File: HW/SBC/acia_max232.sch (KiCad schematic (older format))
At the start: 11 parts, among them J1 Serial Port, U4 MAX232, U5 6551

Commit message: New MB design. Includes RTC. New IDE design.
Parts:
- removed Pad1: RI, Wire_Pads:SolderWirePad_single_0-8mmDrill, symbol Mounting_Hole_PAD
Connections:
- wire segments 59 -> 57
- no-connect marks 6 -> 7
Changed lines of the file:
@@
-$EndComp
-$Comp
-L Mounting_Hole_PAD Pad1
-U 1 1 58D7281F
-P 1475 3200
-F 0 "Pad1" H 1475 3450 50  0000 C CNN
-F 1 "RI" H 1475 3375 50  0000 C CNN
-F 2 "Wire_Pads:SolderWirePad_single_0-8mmDrill" H 1475 3200 50  0001 C CNN
-F 3 "" H 1475 3200 50  0001 C CNN
-	1    1475 3200
-	-1   0    0    1
 $EndComp
 $Comp
@@
 Wire Wire Line
 	3700 3550 3575 3550
-Wire Wire Line
-	1825 2850 1475 2850
-Wire Wire Line
-	1475 2850 1475 3100
 Wire Wire Line
 	4500 4350 4500 4625
@@
 Wire Wire Line
 	7975 4675 7975 4800
+NoConn ~ 1825 2850
 $EndSCHEMATC

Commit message: Updates to pcb and monitor.
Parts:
- added C17: 22pF, Capacitors_ThroughHole:C_Disc_D3.8mm_W2.6mm_P2.50mm, symbol C_Small
- J1: footprint Pin_Headers:Pin_Header_Straight_2x05_Pitch2.54mm -> Connect:IDC_Header_Straight_10pins
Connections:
- net GND: now also C6.1, C17.1; no longer C6.2
- net at U5.6 (XTLI), XTAL1.1: now also C17.2; no longer C6.1
- net at U5.7 (XTLO), XTAL1.2: now also C6.2
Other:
- moved on the sheet: C6
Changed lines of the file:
@@
 L C_Small C6
 U 1 1 58D702B2
-P 6450 2050
-F 0 "C6" H 6550 2100 50  0000 L CNN
-F 1 "22pF" H 6200 2125 50  0000 L CNN
-F 2 "Capacitors_ThroughHole:C_Disc_D3.8mm_W2.6mm_P2.50mm" H 6450 2050 50  0001 C CNN
-F 3 "" H 6450 2050 50  0001 C CNN
-	1    6450 2050
+P 6450 1600
+F 0 "C6" H 6550 1650 50  0000 L CNN
+F 1 "22pF" H 6200 1675 50  0000 L CNN
+F 2 "Capacitors_ThroughHole:C_Disc_D3.8mm_W2.6mm_P2.50mm" H 6450 1600 50  0001 C CNN
+F 3 "" H 6450 1600 50  0001 C CNN
+	1    6450 1600
 	1    0    0    -1
 $EndComp
@@
 L GND #PWR02
 U 1 1 58D7044A
-P 6450 2150
-F 0 "#PWR02" H 6450 1900 50  0001 C CNN
-F 1 "GND" H 6450 2000 50  0000 C CNN
-F 2 "" H 6450 2150 50  0001 C CNN
-F 3 "" H 6450 2150 50  0001 C CNN
-	1    6450 2150
-	1    0    0    -1
+P 6450 1500
+F 0 "#PWR02" H 6450 1250 50  0001 C CNN
+F 1 "GND" H 6450 1350 50  0000 C CNN
+F 2 "" H 6450 1500 50  0001 C CNN
+F 3 "" H 6450 1500 50  0001 C CNN
+	1    6450 1500
+	-1   0    0    1
 $EndComp
 Text GLabel 9150 3925 2    60   Input ~ 0
@@
 F 0 "J1" H 2075 2950 50  0000 C CNN
 F 1 "Serial Port" H 2075 2350 50  0000 C CNN
-F 2 "Pin_Headers:Pin_Header_Straight_2x05_Pitch2.54mm" H 2075 1450 50  0001 C CNN
+F 2 "Connect:IDC_Header_Straight_10pins" H 2075 1450 50  0001 C CNN
 F 3 "" H 2075 1450 50  0001 C CNN
 	1    2075 2650
@@
 	8675 3725 9150 3725
 Wire Wire Line
-	6450 1950 7275 1950
-Connection ~ 6925 1950
+	7275 1700 7275 1950
 Wire Wire Line
 	7275 2075 7150 2075
@@
 	7975 4675 7975 4800
 NoConn ~ 1825 2850
+$Comp
+L C_Small C17
+U 1 1 59018F37
+P 7275 1600
+F 0 "C17" H 7375 1650 50  0000 L CNN
+F 1 "22pF" H 7025 1675 50  0000 L CNN
+F 2 "Capacitors_ThroughHole:C_Disc_D3.8mm_W2.6mm_P2.50mm" H 7275 1600 50  0001 C CNN
+F 3 "" H 7275 1600 50  0001 C CNN
+	1    7275 1600
+	1    0    0    -1
+$EndComp
+$Comp
+L GND #PWR012
+U 1 1 59019537
+P 7275 1500
+F 0 "#PWR012" H 7275 1250 50  0001 C CNN
+F 1 "GND" H 7275 1350 50  0000 C CNN
+F 2 "" H 7275 1500 50  0001 C CNN
+F 3 "" H 7275 1500 50  0001 C CNN
+	1    7275 1500
+	-1   0    0    1
+$EndComp
+Wire Wire Line
+	6925 2150 6450 2150
+Wire Wire Line
+	7275 1950 6925 1950
+Wire Wire Line
+	6450 2150 6450 1700
 $EndSCHEMATC

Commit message: Move dicoupling capacitators as close the chips as possible.
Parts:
- added C?: 0.1uF, symbol C
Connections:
- net GND: now also C?.2
- net VCC: now also C?.1
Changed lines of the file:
@@
 	-1   0    0    1
 $EndComp
-Wire Wire Line
-	8675 1950 9150 1950
-Wire Wire Line
-	8675 2075 9150 2075
-Wire Wire Line
-	8675 2200 9150 2200
-Wire Wire Line
-	8675 2325 9150 2325
-Wire Wire Line
-	8675 2450 9150 2450
-Wire Wire Line
-	8675 2575 9150 2575
-Wire Wire Line
-	8675 2700 9150 2700
-Wire Wire Line
-	8675 2825 9150 2825
-Wire Wire Line
-	8675 3100 9150 3100
-Wire Wire Line
-	8675 3225 9150 3225
-Wire Wire Line
-	8675 3475 9500 3475
-Wire Wire Line
-	8675 3600 9150 3600
-Wire Wire Line
-	8675 3725 9150 3725
-Wire Wire Line
-	7275 1700 7275 1950
-Wire Wire Line
-	7275 2075 7150 2075
-Wire Wire Line
-	7150 2075 6925 2150
-Wire Wire Line
-	8675 4050 9150 4050
-Wire Wire Line
-	8675 4175 9150 4175
-Wire Wire Line
-	8675 3925 9150 3925
-Wire Wire Line
-	5300 4050 5425 4050
-Wire Wire Line
-	5425 3850 5300 3750
-Wire Wire Line
-	3700 4050 3575 4050
-Wire Wire Line
-	3575 3850 3700 3750
-Wire Wire Line
-	3700 3250 3575 3250
-Wire Wire Line
-	3375 3250 3050 3250
-Wire Wire Line
-	1825 2650 1650 2650
-Wire Wire Line
-	1650 2650 1650 3150
-Wire Wire Line
-	3700 3550 3575 3550
-Wire Wire Line
-	4500 4350 4500 4625
-Wire Wire Line
-	3050 4500 4925 4500
-Connection ~ 4500 4500
-Wire Wire Line
-	3375 3550 3050 3550
-Wire Wire Line
-	3050 3550 3050 4500
-Wire Wire Line
-	2325 2450 3700 2450
-Wire Wire Line
-	1825 2550 1725 2550
-Wire Wire Line
-	1725 2550 1725 2275
-Wire Wire Line
-	1725 2275 3475 2275
-Wire Wire Line
-	3475 2275 3475 2850
-Wire Wire Line
-	3475 2850 3700 2850
-Wire Wire Line
-	1825 2750 1750 2750
-Wire Wire Line
-	1750 2750 1750 3050
-Wire Wire Line
-	1750 3050 3700 3050
-Wire Wire Line
-	2325 2750 2925 2750
-Wire Wire Line
-	2925 2750 2925 2650
-Wire Wire Line
-	2925 2650 3700 2650
 NoConn ~ 2325 2550
 NoConn ~ 2325 2650
 NoConn ~ 2325 2850
 NoConn ~ 1825 2450
-Wire Wire Line
-	5300 2450 7275 2450
-Wire Wire Line
-	6650 2300 7275 2300
-Wire Wire Line
-	5300 3050 6850 3050
-Wire Wire Line
-	6850 3050 6850 2700
-Wire Wire Line
-	6850 2700 7275 2700
-Wire Wire Line
-	5300 2650 6300 2650
-Wire Wire Line
-	6300 2650 6300 2900
-Wire Wire Line
-	6300 2900 7275 2900
-Wire Wire Line
-	5300 2850 5925 2850
-Wire Wire Line
-	5925 2850 5925 2550
-Wire Wire Line
-	5925 2550 6650 2550
-Wire Wire Line
-	6650 2550 6650 2300
 $Comp
 L GND #PWR08
@@
 	1    0    0    -1
 $EndComp
-Wire Wire Line
-	7975 4675 7975 4800
 NoConn ~ 1825 2850
 $Comp
@@
 	-1   0    0    1
 $EndComp
+$Comp
+L C C?
+U 1 1 5905372B
+P 8125 4675
+F 0 "C?" V 8275 4625 50  0000 L CNN
+F 1 "0.1uF" V 7975 4650 50  0000 L CNN
+F 2 "" H 8163 4525 50  0001 C CNN
+F 3 "" H 8125 4675 50  0001 C CNN
+	1    8125 4675
+	0    1    1    0
+$EndComp
+Wire Wire Line
+	8675 1950 9150 1950
+Wire Wire Line
+	8675 2075 9150 2075
+Wire Wire Line
+	8675 2200 9150 2200
+Wire Wire Line
+	8675 2325 9150 2325
+Wire Wire Line
+	8675 2450 9150 2450
+Wire Wire Line
+	8675 2575 9150 2575
+Wire Wire Line
+	8675 2700 9150 2700
+Wire Wire Line
+	8675 2825 9150 2825
+Wire Wire Line
+	8675 3100 9150 3100
+Wire Wire Line
+	8675 3225 9150 3225
+Wire Wire Line
+	8675 3475 9500 3475
+Wire Wire Line
+	8675 3600 9150 3600
+Wire Wire Line
+	8675 3725 9150 3725
+Wire Wire Line
+	7275 1700 7275 1950
+Wire Wire Line
+	7275 2075 7150 2075
+Wire Wire Line
+	7150 2075 6925 2150
+Wire Wire Line
+	8675 4050 9150 4050
+Wire Wire Line
+	8675 4175 9150 4175
+Wire Wire Line
+	8675 3925 9150 3925
+Wire Wire Line
+	5300 4050 5425 4050
+Wire Wire Line
+	5425 3850 5300 3750
+Wire Wire Line
+	3700 4050 3575 4050
+Wire Wire Line
+	3575 3850 3700 3750
+Wire Wire Line
+	3700 3250 3575 3250
+Wire Wire Line
+	3375 3250 3050 3250
+Wire Wire Line
+	1825 2650 1650 2650
+Wire Wire Line
+	1650 2650 1650 3150
+Wire Wire Line
+	3700 3550 3575 3550
+Wire Wire Line
+	4500 4350 4500 4625
+Wire Wire Line
+	3050 4500 4925 4500
+Connection ~ 4500 4500
+Wire Wire Line
+	3375 3550 3050 3550
+Wire Wire Line
+	3050 3550 3050 4500
+Wire Wire Line
+	2325 2450 3700 2450
+Wire Wire Line
+	1825 2550 1725 2550
+Wire Wire Line
+	1725 2550 1725 2275
+Wire Wire Line
+	1725 2275 3475 2275
+Wire Wire Line
+	3475 2275 3475 2850
+Wire Wire Line
+	3475 2850 3700 2850
+Wire Wire Line
+	1825 2750 1750 2750
+Wire Wire Line
+	1750 2750 1750 3050
+Wire Wire Line
+	1750 3050 3700 3050
+Wire Wire Line
+	2325 2750 2925 2750
+Wire Wire Line
+	2925 2750 2925 2650
+Wire Wire Line
+	2925 2650 3700 2650
+Wire Wire Line
+	5300 2450 7275 2450
+Wire Wire Line
+	6650 2300 7275 2300
+Wire Wire Line
+	5300 3050 6850 3050
+Wire Wire Line
+	6850 3050 6850 2700
+Wire Wire Line
+	6850 2700 7275 2700
+Wire Wire Line
+	5300 2650 6300 2650
+Wire Wire Line
+	6300 2650 6300 2900
+Wire Wire Line
+	6300 2900 7275 2900
+Wire Wire Line
+	5300 2850 5925 2850
+Wire Wire Line
+	5925 2850 5925 2550
+Wire Wire Line
+	5925 2550 6650 2550
+Wire Wire Line
+	6650 2550 6650 2300
+Wire Wire Line
+	7975 4675 7975 4800
 Wire Wire Line
 	6925 2150 6450 2150
@@
 Wire Wire Line
 	6450 2150 6450 1700
+Connection ~ 7975 1600
+Wire Wire Line
+	8275 4675 9725 4675
+Wire Wire Line
+	9725 4675 9725 1600
+Wire Wire Line
+	9725 1600 7975 1600
 $EndSCHEMATC

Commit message: Schema changes to SBC
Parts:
- C12: renamed from C?; footprint (none) -> Capacitors_ThroughHole:C_Disc_D3.8mm_W2.6mm_P2.50mm
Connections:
- no-connect marks 7 -> 8
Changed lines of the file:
@@
 $EndComp
 $Comp
-L C C?
+L C C12
 U 1 1 5905372B
 P 8125 4675
-F 0 "C?" V 8275 4625 50  0000 L CNN
+F 0 "C12" V 8275 4625 50  0000 L CNN
 F 1 "0.1uF" V 7975 4650 50  0000 L CNN
-F 2 "" H 8163 4525 50  0001 C CNN
+F 2 "Capacitors_ThroughHole:C_Disc_D3.8mm_W2.6mm_P2.50mm" H 8163 4525 50  0001 C CNN
 F 3 "" H 8125 4675 50  0001 C CNN
 	1    8125 4675
@@
 Wire Wire Line
 	9725 1600 7975 1600
+NoConn ~ 7325 3950
 $EndSCHEMATC

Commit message: New board layout. WIP
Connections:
- net GND: no longer C12.2, U5.1 (GND)
- net VCC: no longer C12.1, C2.2, C4.1, U4.16 (VCC), U5.15 (VCC)
- new net: C12.2, U5.1 (GND)
- new net: C12.1, U5.15 (VCC)
- new net: C2.2, C4.1, U4.16 (VCC)
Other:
- moved on the sheet: C4
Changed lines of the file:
@@
 L CP1_Small C4
 U 1 1 58D70C29
-P 4925 4600
-F 0 "C4" H 4935 4670 50  0000 L CNN
-F 1 "10uF" H 4935 4520 50  0000 L CNN
-F 2 "Capacitors_ThroughHole:CP_Radial_D5.0mm_P2.50mm" H 4925 4600 50  0001 C CNN
-F 3 "" H 4925 4600 50  0001 C CNN
-	1    4925 4600
+P 4500 4450
+F 0 "C4" H 4510 4520 50  0000 L CNN
+F 1 "10uF" H 4510 4370 50  0000 L CNN
+F 2 "Capacitors_ThroughHole:CP_Radial_D5.0mm_P2.50mm" H 4500 4450 50  0001 C CNN
+F 3 "" H 4500 4450 50  0001 C CNN
+	1    4500 4450
 	1    0    0    -1
 $EndComp
@@
 $EndComp
 $Comp
-L VCC #PWR04
-U 1 1 58D7177E
-P 4500 4625
-F 0 "#PWR04" H 4500 4475 50  0001 C CNN
-F 1 "VCC" H 4500 4775 50  0000 C CNN
-F 2 "" H 4500 4625 50  0001 C CNN
-F 3 "" H 4500 4625 50  0001 C CNN
-	1    4500 4625
-	-1   0    0    1
-$EndComp
-$Comp
 L CONN_02X05 J1
 U 1 1 58D71D6B
@@
 L GND #PWR06
 U 1 1 58D72DB3
-P 4925 4700
-F 0 "#PWR06" H 4925 4450 50  0001 C CNN
-F 1 "GND" H 4925 4550 50  0000 C CNN
-F 2 "" H 4925 4700 50  0001 C CNN
-F 3 "" H 4925 4700 50  0001 C CNN
-	1    4925 4700
+P 4500 4550
+F 0 "#PWR06" H 4500 4300 50  0001 C CNN
+F 1 "GND" H 4500 4400 50  0000 C CNN
+F 2 "" H 4500 4550 50  0001 C CNN
+F 3 "" H 4500 4550 50  0001 C CNN
+	1    4500 4550
 	1    0    0    -1
 $EndComp
@@
 NoConn ~ 7275 3275
 NoConn ~ 7275 4175
-$Comp
-L GND #PWR010
-U 1 1 58D84381
-P 7975 4800
-F 0 "#PWR010" H 7975 4550 50  0001 C CNN
-F 1 "GND" H 7975 4650 50  0000 C CNN
-F 2 "" H 7975 4800 50  0001 C CNN
-F 3 "" H 7975 4800 50  0001 C CNN
-	1    7975 4800
-	1    0    0    -1
-$EndComp
-$Comp
-L VCC #PWR011
-U 1 1 58D845E7
-P 7975 1600
-F 0 "#PWR011" H 7975 1450 50  0001 C CNN
-F 1 "VCC" H 7975 1750 50  0000 C CNN
-F 2 "" H 7975 1600 50  0001 C CNN
-F 3 "" H 7975 1600 50  0001 C CNN
-	1    7975 1600
-	1    0    0    -1
-$EndComp
 NoConn ~ 1825 2850
 $Comp
@@
 	0    1    1    0
 $EndComp
+NoConn ~ 7325 3950
 Wire Wire Line
 	8675 1950 9150 1950
@@
 	3700 3550 3575 3550
 Wire Wire Line
-	4500 4350 4500 4625
-Wire Wire Line
-	3050 4500 4925 4500
-Connection ~ 4500 4500
-Wire Wire Line
 	3375 3550 3050 3550
 Wire Wire Line
-	3050 3550 3050 4500
+	3050 3550 3050 4350
 Wire Wire Line
 	2325 2450 3700 2450
@@
 	6650 2550 6650 2300
 Wire Wire Line
-	7975 4675 7975 4800
-Wire Wire Line
 	6925 2150 6450 2150
 Wire Wire Line
@@
 Wire Wire Line
 	6450 2150 6450 1700
-Connection ~ 7975 1600
-Wire Wire Line
-	8275 4675 9725 4675
-Wire Wire Line
-	9725 4675 9725 1600
-Wire Wire Line
-	9725 1600 7975 1600
-NoConn ~ 7325 3950
+Wire Wire Line
+	8275 4675 9650 4675
+Wire Wire Line
+	9650 4675 9650 1600
+Wire Wire Line
+	9650 1600 7975 1600
+Wire Wire Line
+	4500 4350 3050 4350
 $EndSCHEMATC

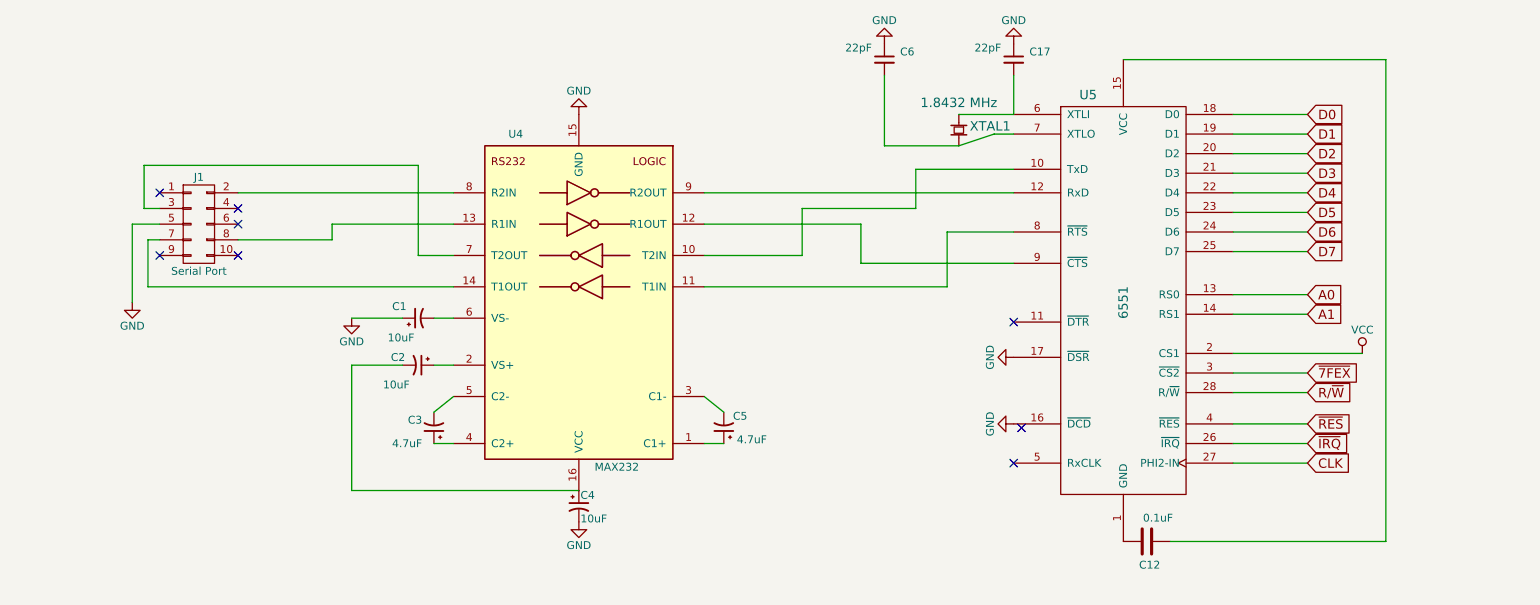
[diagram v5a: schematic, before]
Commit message: New SBC PCB. Started to split pluto_kernel.asm into bios, monitor and miniassembler/disassembler. Various other updates.
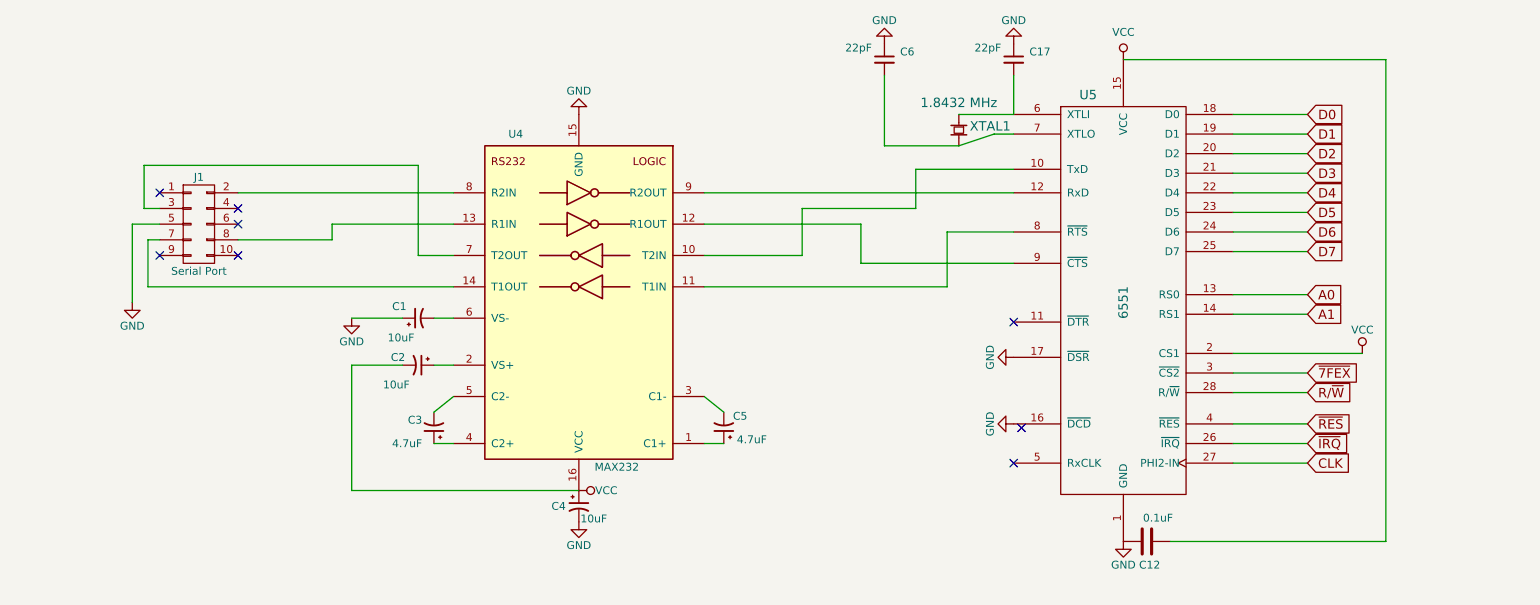
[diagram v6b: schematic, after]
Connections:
- net GND: now also C12.2, U5.1 (GND)
- net VCC: now also C12.1, C2.2, C4.1, U4.16 (VCC), U5.15 (VCC)
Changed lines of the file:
@@
 U 1 1 58D70C29
 P 4500 4450
-F 0 "C4" H 4510 4520 50  0000 L CNN
+F 0 "C4" H 4325 4450 50  0000 L CNN
 F 1 "10uF" H 4510 4370 50  0000 L CNN
 F 2 "Capacitors_ThroughHole:CP_Radial_D5.0mm_P2.50mm" H 4500 4450 50  0001 C CNN
@@
 $EndComp
 $Comp
-L GND #PWR05
+L GND #PWR04
 U 1 1 58D71F12
 P 1650 3150
-F 0 "#PWR05" H 1650 2900 50  0001 C CNN
+F 0 "#PWR04" H 1650 2900 50  0001 C CNN
 F 1 "GND" H 1650 3000 50  0000 C CNN
 F 2 "" H 1650 3150 50  0001 C CNN
@@
 $EndComp
 $Comp
-L GND #PWR06
+L GND #PWR05
 U 1 1 58D72DB3
 P 4500 4550
-F 0 "#PWR06" H 4500 4300 50  0001 C CNN
+F 0 "#PWR05" H 4500 4300 50  0001 C CNN
 F 1 "GND" H 4500 4400 50  0000 C CNN
 F 2 "" H 4500 4550 50  0001 C CNN
@@
 $EndComp
 $Comp
-L GND #PWR07
+L GND #PWR06
 U 1 1 58D73252
 P 4500 1950
-F 0 "#PWR07" H 4500 1700 50  0001 C CNN
+F 0 "#PWR06" H 4500 1700 50  0001 C CNN
 F 1 "GND" H 4500 1800 50  0000 C CNN
 F 2 "" H 4500 1950 50  0001 C CNN
@@
 NoConn ~ 1825 2450
 $Comp
-L GND #PWR08
+L GND #PWR07
 U 1 1 58D744C7
 P 7275 3925
-F 0 "#PWR08" H 7275 3675 50  0001 C CNN
+F 0 "#PWR07" H 7275 3675 50  0001 C CNN
 F 1 "GND" H 7275 3775 50  0000 C CNN
 F 2 "" H 7275 3925 50  0001 C CNN
@@
 $EndComp
 $Comp
-L GND #PWR09
+L GND #PWR08
 U 1 1 58D74507
 P 7275 3500
-F 0 "#PWR09" H 7275 3250 50  0001 C CNN
+F 0 "#PWR08" H 7275 3250 50  0001 C CNN
 F 1 "GND" H 7275 3350 50  0000 C CNN
 F 2 "" H 7275 3500 50  0001 C CNN
@@
 $EndComp
 $Comp
-L GND #PWR012
+L GND #PWR09
 U 1 1 59019537
 P 7275 1500
-F 0 "#PWR012" H 7275 1250 50  0001 C CNN
+F 0 "#PWR09" H 7275 1250 50  0001 C CNN
 F 1 "GND" H 7275 1350 50  0000 C CNN
 F 2 "" H 7275 1500 50  0001 C CNN
@@
 	9650 1600 7975 1600
 Wire Wire Line
-	4500 4350 3050 4350
+	3050 4350 4500 4350
+$Comp
+L GND #PWR?
+U 1 1 5924C9C7
+P 7975 4675
+F 0 "#PWR?" H 7975 4425 50  0001 C CNN
+F 1 "GND" H 7975 4525 50  0000 C CNN
+F 2 "" H 7975 4675 50  0001 C CNN
+F 3 "" H 7975 4675 50  0001 C CNN
+	1    7975 4675
+	1    0    0    -1
+$EndComp
+$Comp
+L VCC #PWR?
+U 1 1 5924CA70
+P 4500 4350
+F 0 "#PWR?" H 4500 4200 50  0001 C CNN
+F 1 "VCC" V 4500 4525 50  0000 C CNN
+F 2 "" H 4500 4350 50  0001 C CNN
+F 3 "" H 4500 4350 50  0001 C CNN
+	1    4500 4350
+	0    1    1    0
+$EndComp
+$Comp
+L VCC #PWR?
+U 1 1 5924CC0E
+P 7975 1600
+F 0 "#PWR?" H 7975 1450 50  0001 C CNN
+F 1 "VCC" H 7975 1775 50  0000 C CNN
+F 2 "" H 7975 1600 50  0001 C CNN
+F 3 "" H 7975 1600 50  0001 C CNN
+	1    7975 1600
+	1    0    0    -1
+$EndComp
 $EndSCHEMATC
